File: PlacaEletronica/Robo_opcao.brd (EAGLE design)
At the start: 139.7 x 148 mm, 101 parts, among them IC1 7805DT, IC2 7805DT, J1 F-1X06-SIP-100-40, J2 S2B-PH-K-S(LF)(SN), J3 ZX62-B-5PA, Q1 SMD-TRANSISTORS-NPN-25V-500MW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, Q2 SMD-TRANSISTORS-NPN-25V-500MW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, Q4 SFH_3716, Q5 TSOP4838, U1 ESP32-WROOM-32D, U2 AMS1117-3.3, U3 INTERFACE-CP2102-GMR(QFN28)QF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

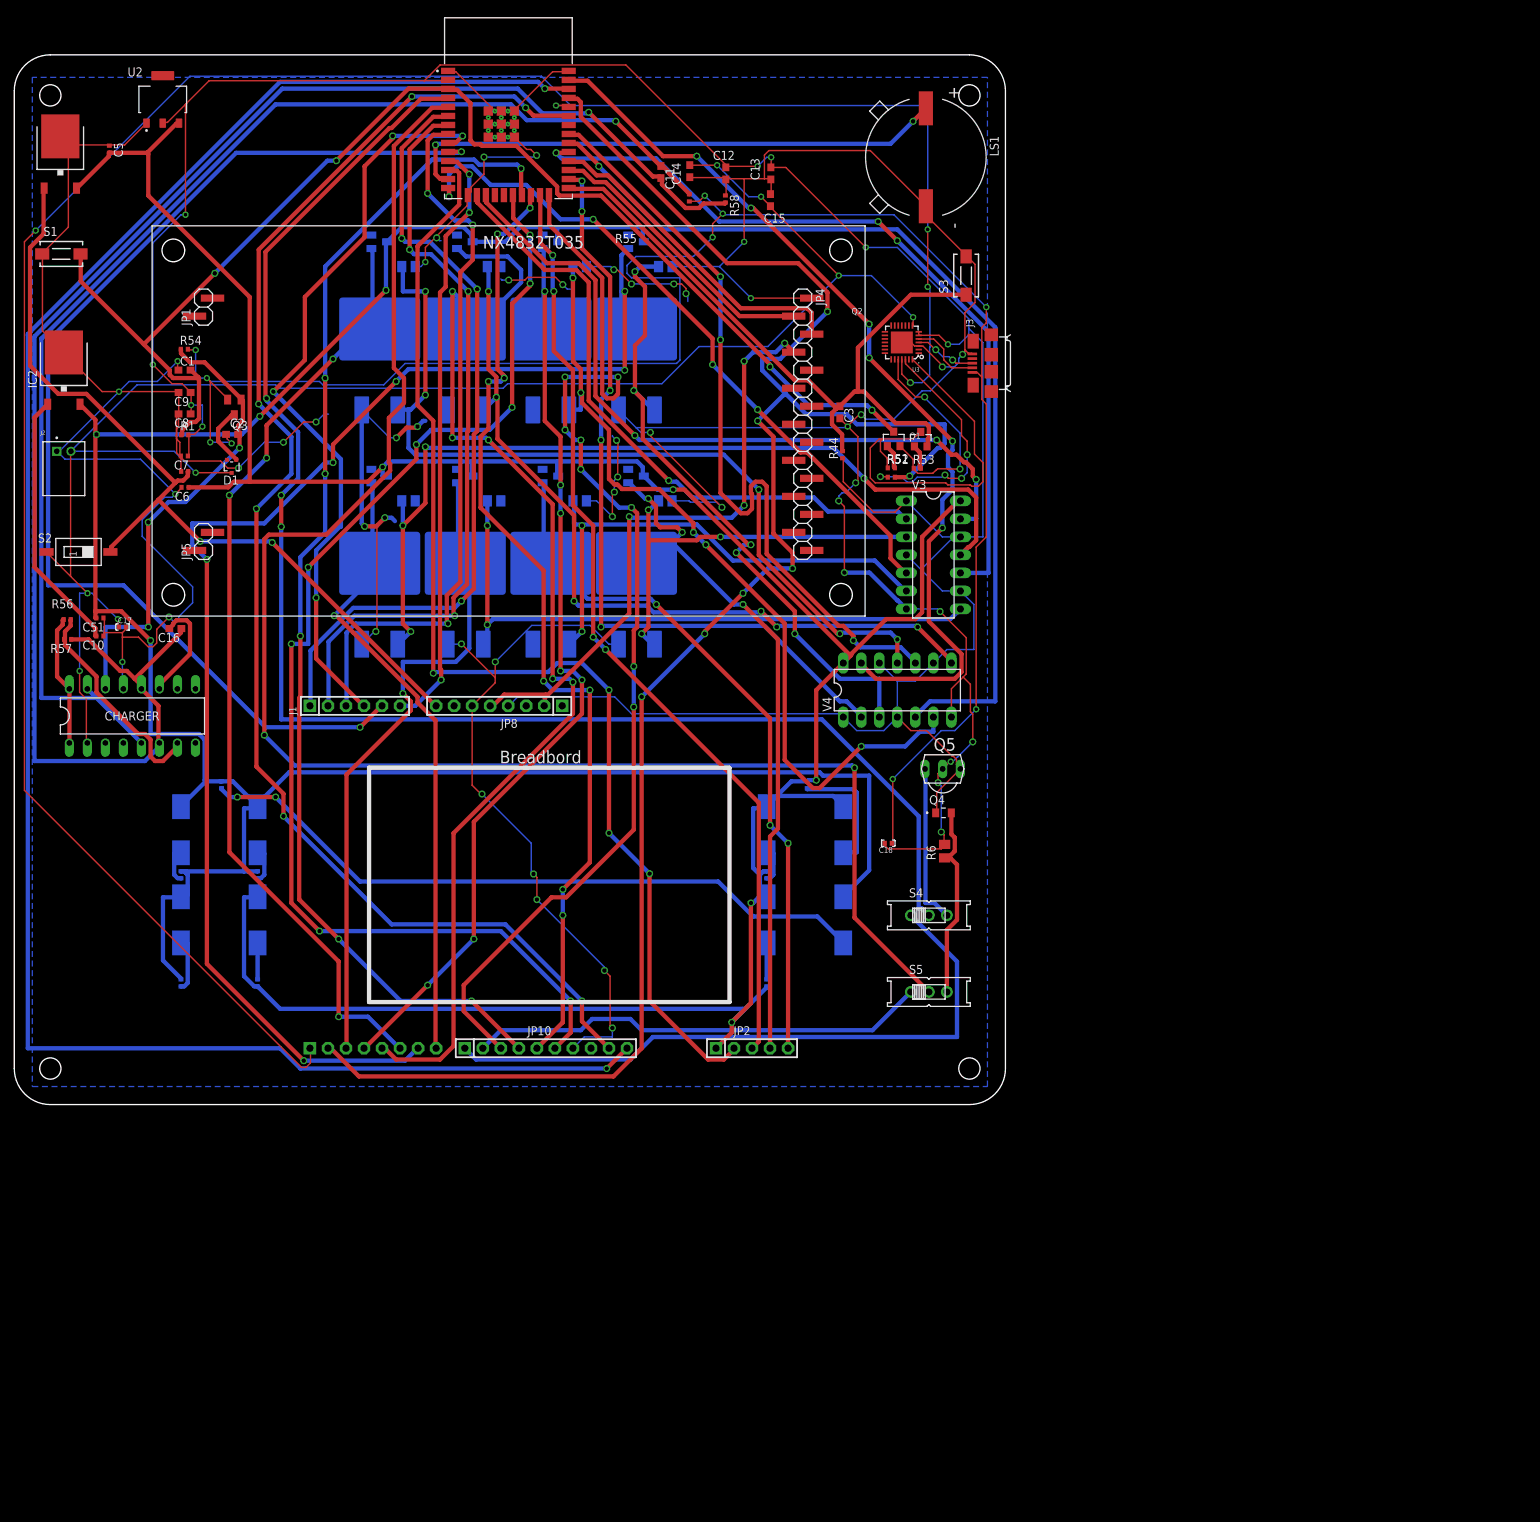
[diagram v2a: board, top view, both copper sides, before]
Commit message: [MODIFIED] Troca de pinagem na placa principal
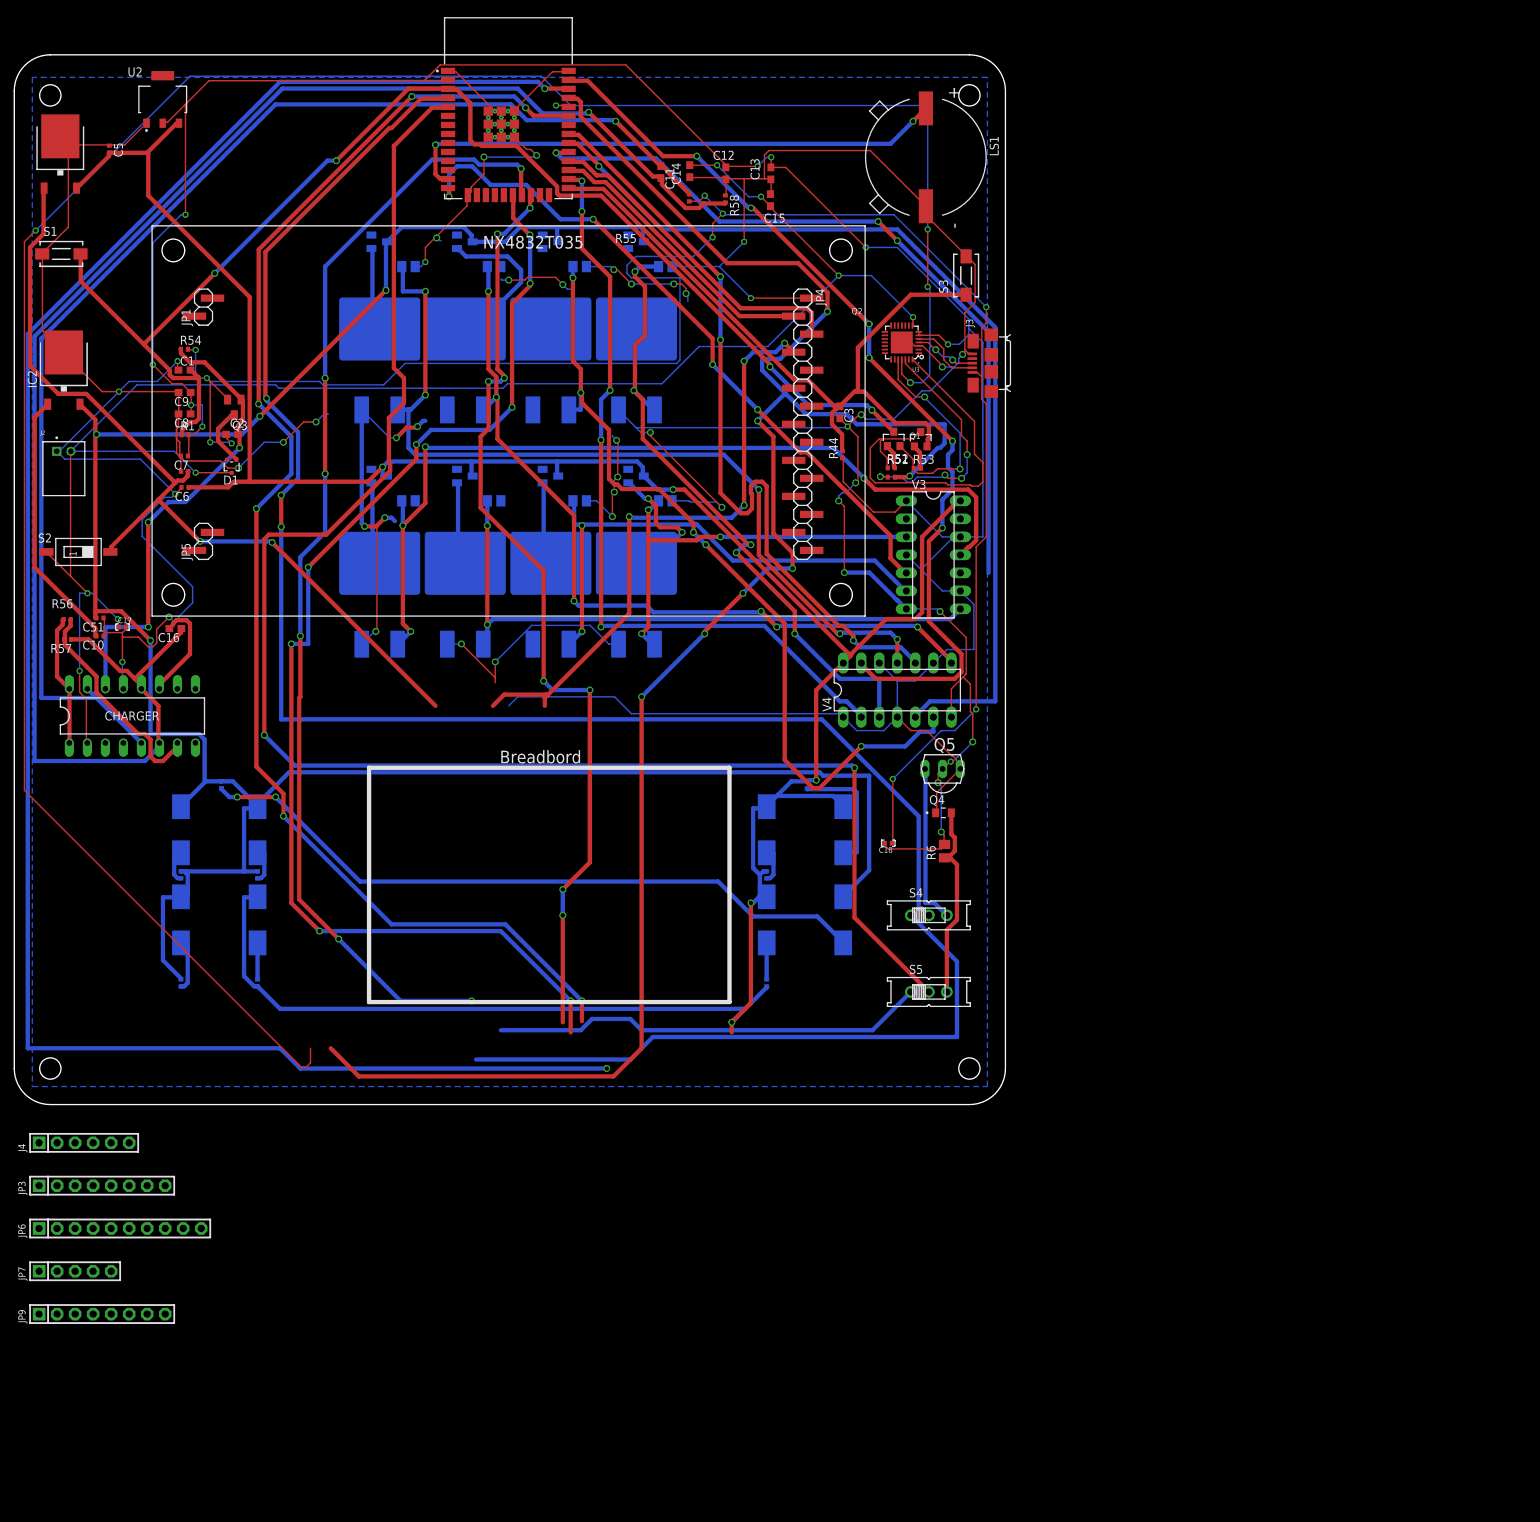
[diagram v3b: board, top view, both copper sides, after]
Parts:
- removed J1: F-1X06-SIP-100-40, con-headers-jp(1):SIP-100-06-40
- removed JP10: F-1X10-SIP-100-40, con-headers-jp(1):SIP-100-10-40
- removed JP11, JP8: F-1X08-SIP-100-40, con-headers-jp(1):SIP-100-08-40
- removed JP2: F-1X05-SIP-100-40, con-headers-jp(1):SIP-100-05-40
- added J4: F-1X06-SIP-100-40, con-headers-jp(1):SIP-100-06-40
- added JP3, JP9: F-1X08-SIP-100-40, con-headers-jp(1):SIP-100-08-40
- added JP6: F-1X10-SIP-100-40, con-headers-jp(1):SIP-100-10-40
- added JP7: F-1X05-SIP-100-40, con-headers-jp(1):SIP-100-05-40
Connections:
- removed net 10(5V): U1.14, V3.5
- removed net 11(5V): U1.29, V3.10
- removed net 12(5V): U1.17, V3.13
- removed net 13(5V): U1.26, V4.2
- removed net 1_S: J1.1, U1.6
- removed net 2_S: J1.2, U1.7
- removed net 3_S: J1.3, U1.8
- removed net 4_S: J1.4, U1.9
- removed net 5_S: J1.5, U1.10
- removed net 6_S: J1.6, U1.11
- removed net 7_S: JP2.2, U1.12
- removed net 8_S: JP2.3, U1.23
- removed net 9(5V): U1.16, V3.2
- removed net N$29: JP8.1
- removed net N$48: JP10.8
- removed net PORT_10~5V: D11.1, JP2.5, U$12.2
- removed net PORT_11~5V: D12.1, JP11.3, U$13.2
- removed net PORT_12~5V: D13.1, JP11.8, U$14.2
- removed net PORT_13~5V: D14.1, JP11.7, U$15.2
- removed net PORT_9~5V: D10.1, JP2.4, U$11.2
- removed net PWM1(5V): U1.30, V4.5
- removed net PWM2(5V): U1.31, V4.10
- removed net PWM3(5V): U1.37, V4.13
- removed net PWM_1~5V: D15.1, JP11.4, U$16.2
- removed net PWM_2~5V: D16.1, JP11.5, U$17.2
- removed net PWM_3~5V: D17.1, JP11.6, U$18.2
- removed net SS: JP10.3, U1.24
- new net 5V(ATENçãO)-NãOESTACONECTADOEMNDA: JP9.5
- new net 5V(NAOTACONECTADOEMNDA): JP9.2
- new net IO12: J4.3, U1.14
- new net IO13: J4.4, U1.16
- new net IO15: U1.23, V4.5
- new net IO15-5V: D15.1, JP6.2, U$16.2
- new net IO18-SPI: JP6.6, U1.30
- new net IO19-SPI: JP6.5, U1.31
- new net IO2: J4.1, U1.24
- new net IO23-SPI: JP6.4, U1.37
- new net IO25: U1.10, V3.2
- new net IO25-5V: D10.1, JP3.3, U$11.2
- new net IO26: U1.11, V3.5
- new net IO26-5V: D11.1, JP3.4, U$12.2
- new net IO27: U1.12, V3.10
- new net IO27-5V: D12.1, JP3.5, U$13.2
- new net IO32: U1.8, V3.13
- new net IO32-5V: D13.1, JP3.6, U$14.2
- new net IO33: U1.9, V4.2
- new net IO33-5V: D14.1, JP3.7, U$15.2
- new net IO34: U1.6, V4.10
- new net IO34-5V: D16.1, JP3.8, U$17.2
- new net IO35: U1.7, V4.13
- new net IO35-5V: D17.1, JP6.1, U$18.2
- new net IO4: J4.2, U1.26
- new net IO5-SPI: JP6.3, U1.29
- new net RESET: JP6.8, JP9.3
- net 5V: no longer JP8.2, JP8.5
- net GND: now also JP6.7, JP9.6, JP9.7; no longer JP10.7, JP8.6, JP8.7
- net GND_PWM~5V: no longer JP2.1
- net I2C_SCL: now also JP6.10; no longer JP10.10
- net I2C_SDA: now also JP6.9; no longer JP10.9
- net MISO: no longer JP10.5
- net MOSI: no longer JP10.4
- net RX0: now also JP3.1; no longer JP11.1
- net SCK: no longer JP10.6
- net TX0: now also JP3.2; no longer JP11.2
- net VDD33: now also JP9.4; no longer JP8.4
- net VIN: now also JP9.8; no longer JP8.8
- net VN_SENSOR_IN: now also J4.6; no longer JP10.2
- net VP_SENSOR_IN: now also J4.5; no longer JP10.1
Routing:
- net PORT_13~5V: track 196.0 -> 0.00 mm, vias 6 -> 0
- net PWM_2~5V: track 166.2 -> 0.00 mm, vias 5 -> 0
- net 7_S: track 164.8 -> 0.00 mm, vias 4 -> 0
- net 5_S: track 162.2 -> 0.00 mm, vias 2 -> 0
- net SS: track 157.5 -> 0.00 mm, vias 8 -> 0
- net PWM_3~5V: track 136.4 -> 0.00 mm, vias 4 -> 0
- net PWM1(5V): track 136.0 -> 0.00 mm, vias 1 -> 0
- net IO18-SPI: track 0.00 -> 135.8 mm, vias 0 -> 1
- net PWM_1~5V: track 135.3 -> 0.00 mm, vias 7 -> 0
- net 8_S: track 133.5 -> 0.00 mm, vias 4 -> 0
- net PWM3(5V): track 130.0 -> 0.00 mm, vias 6 -> 0
- net IO23-SPI: track 0.00 -> 129.8 mm, vias 0 -> 6
- net 1_S: track 111.7 -> 0.00 mm, vias 3 -> 0
- net 11(5V): track 111.2 -> 0.00 mm, vias 3 -> 0
- net PWM2(5V): track 109.4 -> 0.00 mm, vias 3 -> 0
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
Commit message: [MODIFIED] Borda superior da placa, posicao e sentido pin heads
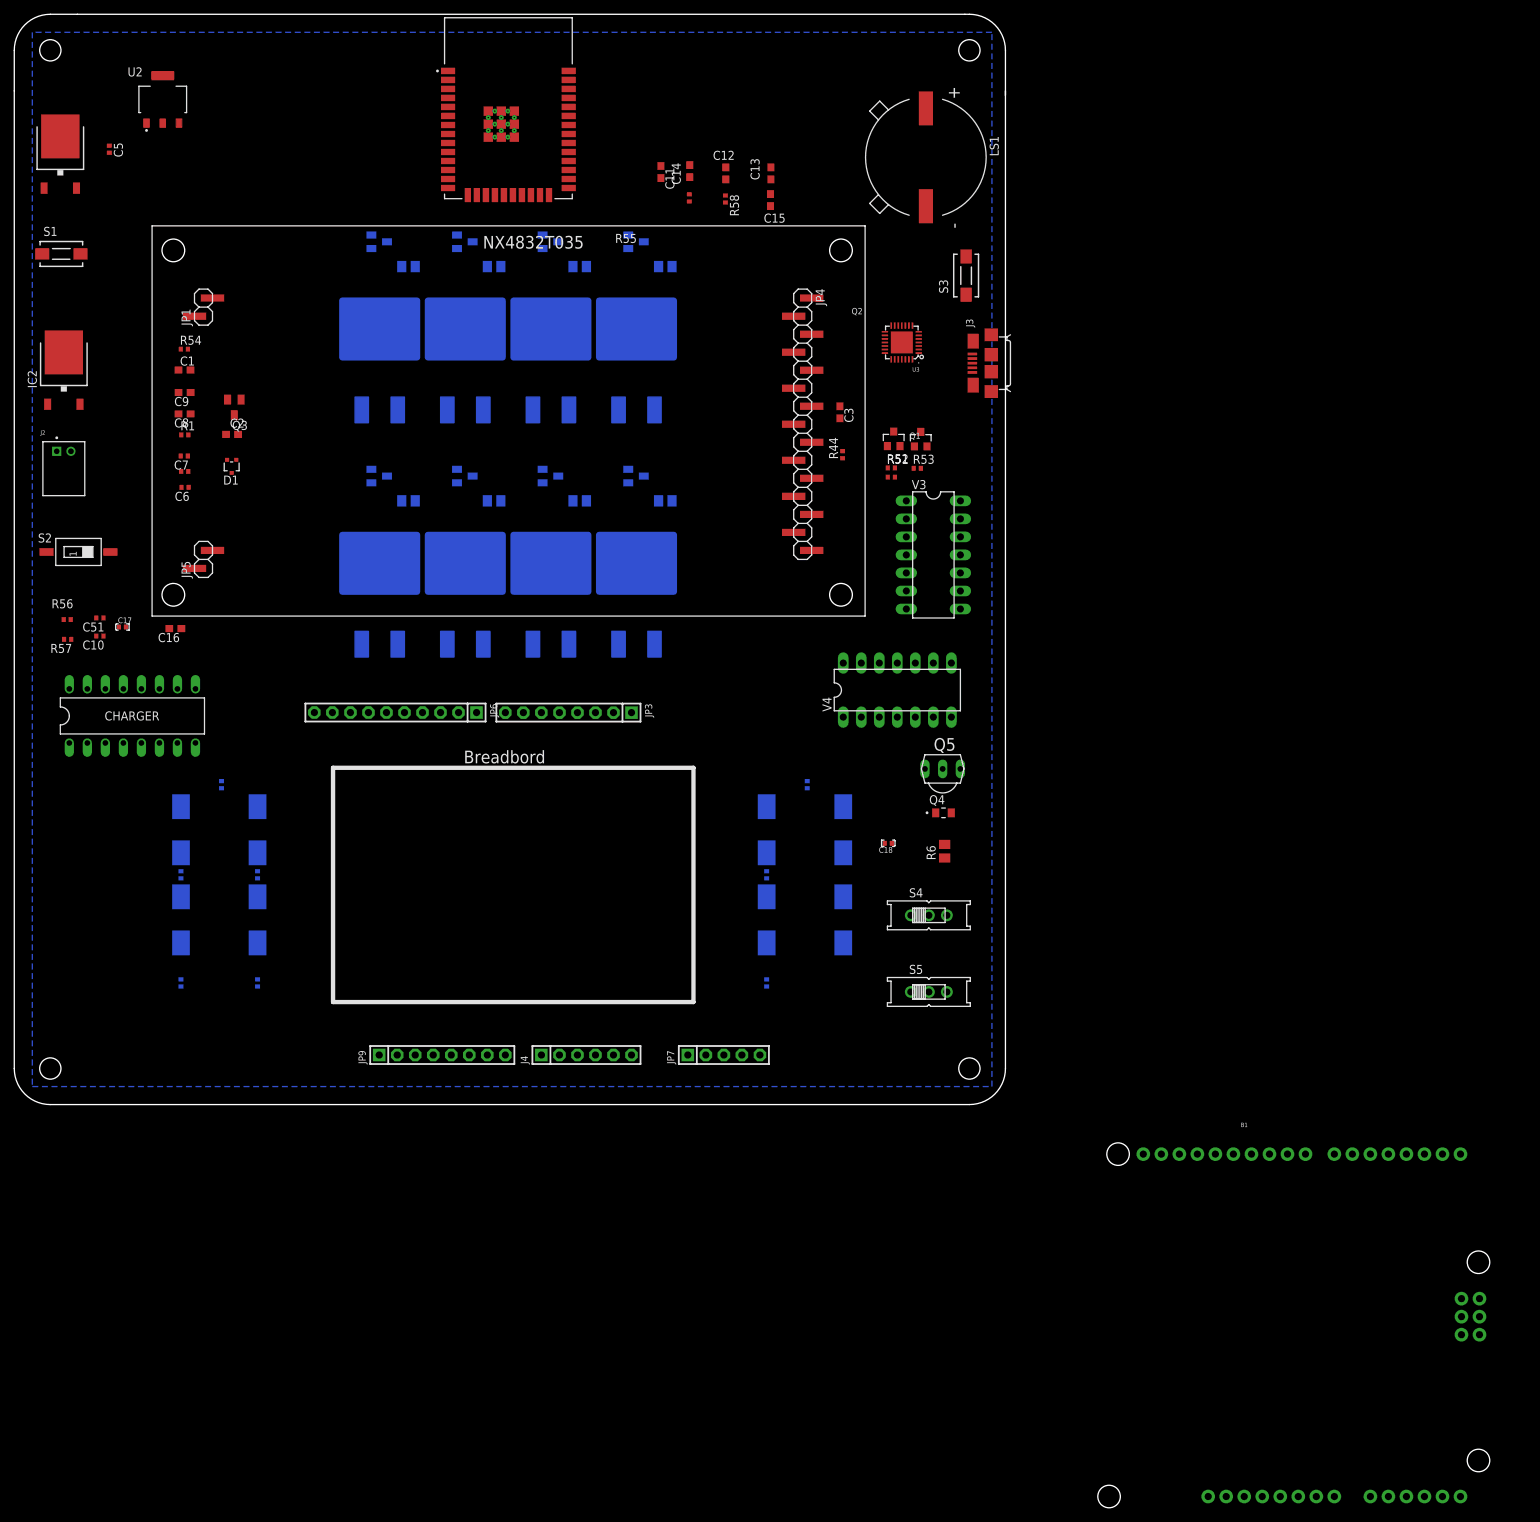
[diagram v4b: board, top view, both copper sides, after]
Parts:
- added B1: ARDUINO_UNO_R3, SparkFun-Boards:ARDUINO_R3
- moved JP7 96.4 mm to (100.0, 6.99)
- moved JP3 93.6 mm to (78.1, 55.2), turned to 180 degrees
- moved JP6 82.4 mm to (53.7, 55.3), turned to 180 degrees
- moved J4 71.9 mm to (80.6, 6.99)
- moved JP9 60.3 mm to (60.3, 6.99)
- moved JP5 2.54 mm to (26.7, 76.8)
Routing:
- net GND: track 680.6 -> 0.00 mm, vias 45 -> 0
- net VDD33: track 390.2 -> 0.00 mm, vias 8 -> 0
- net GND_PWM~5V: track 384.6 -> 0.00 mm, vias 5 -> 0
- net GND_PWM~5V1(2): track 330.2 -> 0.00 mm, vias 4 -> 0
- net RX0: track 324.0 -> 0.00 mm, vias 5 -> 0
- net I2C_SCL: track 274.8 -> 0.00 mm, vias 2 -> 0
- net DC_IN: track 264.0 -> 0.00 mm, vias 10 -> 0
- net TX0: track 259.8 -> 0.00 mm, vias 7 -> 0
- net B+: track 240.2 -> 0.00 mm, vias 8 -> 0
- net B-: track 230.2 -> 0.00 mm, vias 1 -> 0
- net VN_SENSOR: track 227.7 -> 0.00 mm, vias 2 -> 0
- net VP_SENSOR: track 213.9 -> 0.00 mm, vias 3 -> 0
- net I2C_SDA: track 194.9 -> 0.00 mm, vias 6 -> 0
- net EN: track 182.1 -> 0.00 mm, vias 4 -> 0
- net V+: track 179.6 -> 0.00 mm, vias 1 -> 0
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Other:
- board size 139.7 x 148 mm -> 139.7 x 153.7 mm
